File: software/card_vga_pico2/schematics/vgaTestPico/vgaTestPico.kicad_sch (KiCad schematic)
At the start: 31 parts, among them J10 Conn_02x37_Row_Letter_Last, U2 74HC138, U3 74HC139, U4 74HC245, U5 74HC245

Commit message: Schematic update
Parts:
- removed R5: 1k, symbol Device:R
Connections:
- net /AS is gone; now on net C./AS: R22.2
- net /LDS is gone; now on net C./LDS: R21.2
- net C.R/W: now also R20.2
- net /WRL: no longer R20.2
- net at U4.1 (A->B): now also U1.13 (GND), U1.18 (GND), U1.23 (GND), U1.28 (GND), U1.3 (GND), U1.33 (GND), U1.38 (GND), U1.8 (GND), U2.8 (GND), U3.13 (A1), U3.14 (A0), U3.15 (E), U3.8 (GND), U4.10 (GND), U4.19 (CE), U5.1 (A->B), U5.10 (GND), U5.11 (B7), U5.12 (B6), U5.13 (B5), U5.19 (CE), U5.7 (A5), U5.8 (A6), U5.9 (A7)
- net at U2.5 (~{E1}): now also U3.4 (O0)
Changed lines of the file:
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@@
 	)
 	(junction
+		(at 53.34 137.16)
+		(diameter 0)
+		(color 0 0 0 0)
+	)
+	(junction
 		(at 83.82 139.7)
 		(diameter 0)
@@
 	)
 	(junction
+		(at 53.34 142.24)
+		(diameter 0)
+		(color 0 0 0 0)
+	)
+	(junction
+		(at 83.82 147.32)
+		(diameter 0)
+		(color 0 0 0 0)
+	)
+	(junction
+		(at 83.82 99.06)
+		(diameter 0)
+		(color 0 0 0 0)
+	)
+	(junction
+		(at 53.34 139.7)
+		(diameter 0)
+		(color 0 0 0 0)
+	)
+	(junction
 		(at 83.82 137.16)
 		(diameter 0)
@@
 	(wire
 		(pts
-			(xy 83.82 142.24) (xy 83.82 149.86)
+			(xy 83.82 142.24) (xy 83.82 147.32)
 		)
 		(stroke
@@
 	(wire
 		(pts
+			(xy 83.82 96.52) (xy 83.82 99.06)
+		)
+		(stroke
+			(width 0)
+			(type default)
+		)
+	)
+	(wire
+		(pts
 			(xy 228.6 110.49) (xy 245.11 110.49)
 		)
@@
 	(wire
 		(pts
+			(xy 83.82 147.32) (xy 83.82 149.86)
+		)
+		(stroke
+			(width 0)
+			(type default)
+		)
+	)
+	(wire
+		(pts
 			(xy 33.02 124.46) (xy 39.37 124.46)
 		)
@@
 		)
 	)
+	(wire
+		(pts
+			(xy 81.28 96.52) (xy 83.82 96.52)
+		)
+		(stroke
+			(width 0)
+			(type default)
+		)
+	)
 	(bus
 		(pts
@@
 	(wire
 		(pts
+			(xy 53.34 142.24) (xy 53.34 160.02)
+		)
+		(stroke
+			(width 0)
+			(type default)
+		)
+	)
+	(wire
+		(pts
 			(xy 156.21 60.96) (xy 156.21 168.91)
 		)
@@
 		)
 	)
+	(wire
+		(pts
+			(xy 81.28 147.32) (xy 83.82 147.32)
+		)
+		(stroke
+			(width 0)
+			(type default)
+		)
+	)
 	(bus
 		(pts
@@
 		)
 	)
+	(wire
+		(pts
+			(xy 53.34 142.24) (xy 55.88 142.24)
+		)
+		(stroke
+			(width 0)
+			(type default)
+		)
+	)
 	(bus
 		(pts
@@
 	(wire
 		(pts
+			(xy 53.34 139.7) (xy 53.34 142.24)
+		)
+		(stroke
+			(width 0)
+			(type default)
+		)
+	)
+	(wire
+		(pts
 			(xy 228.6 46.99) (xy 245.11 46.99)
 		)
@@
 	(wire
 		(pts
-			(xy 186.69 78.74) (xy 190.5 78.74)
+			(xy 186.69 78.74) (xy 209.55 78.74)
 		)
 		(stroke
@@
 	(wire
 		(pts
+			(xy 53.34 137.16) (xy 55.88 137.16)
+		)
+		(stroke
+			(width 0)
+			(type default)
+		)
+	)
+	(wire
+		(pts
 			(xy 228.6 95.25) (xy 245.11 95.25)
 		)
@@
 	(wire
 		(pts
+			(xy 53.34 137.16) (xy 53.34 139.7)
+		)
+		(stroke
+			(width 0)
+			(type default)
+		)
+	)
+	(wire
+		(pts
 			(xy 81.28 81.28) (xy 104.14 81.28)
 		)
@@
 	(wire
 		(pts
-			(xy 228.6 64.77) (xy 245.11 64.77)
+			(xy 53.34 139.7) (xy 55.88 139.7)
 		)
 		(stroke
@@
 		)
 	)
-	(bus
+	(wire
 		(pts
-			(xy 226.06 92.71) (xy 226.06 95.25)
+			(xy 228.6 64.77) (xy 245.11 64.77)
 		)
 		(stroke
@@
 		)
 	)
-	(wire
+	(bus
 		(pts
-			(xy 198.12 78.74) (xy 209.55 78.74)
+			(xy 226.06 92.71) (xy 226.06 95.25)
 		)
 		(stroke
@@
 	(wire
 		(pts
-			(xy 53.34 106.68) (xy 53.34 160.02)
+			(xy 53.34 106.68) (xy 53.34 137.16)
 		)
 		(stroke
@@
 		)
 	)
-	(global_label "{slash}AS"
+	(global_label "C.{slash}AS"
 		(shape input)
 		(at 207.01 107.95 0)
@@
 		)
 		(property "Intersheetrefs" "${INTERSHEET_REFS}"
-			(at 213.6238 107.95 0)
-			(effects
-				(font
-					(size 1.27 1.27)
-				)
-				(justify left)
-				(hide yes)
-			)
-		)
-	)
-	(global_label "{slash}WRL"
-		(shape input)
-		(at 207.01 100.33 0)
-		(fields_autoplaced yes)
-		(effects
-			(font
-				(size 1.27 1.27)
-			)
-			(justify left)
-		)
-		(property "Intersheetrefs" "${INTERSHEET_REFS}"
-			(at 215.0752 100.33 0)
+			(at 215.4986 107.95 0)
 			(effects
 				(font
@@
 		)
 	)
-	(global_label "{slash}LDS"
+	(global_label "C.{slash}LDS"
 		(shape input)
 		(at 207.01 102.87 0)
@@
 		)
 		(property "Intersheetrefs" "${INTERSHEET_REFS}"
-			(at 214.8333 102.87 0)
+			(at 216.7081 102.87 0)
 			(effects
 				(font
@@
 		)
 	)
+	(global_label "C.R{slash}W"
+		(shape input)
+		(at 207.01 100.33 0)
+		(fields_autoplaced yes)
+		(effects
+			(font
+				(size 1.27 1.27)
+			)
+			(justify left)
+		)
+		(property "Intersheetrefs" "${INTERSHEET_REFS}"
+			(at 215.9219 100.33 0)
+			(effects
+				(font
+					(size 1.27 1.27)
+				)
+				(justify left)
+				(hide yes)
+			)
+		)
+	)
 	(hierarchical_label "A[1..23]"
 		(shape input)
@@
 					(unit 1)
 				)
-			)
-		)
-	)
-	(symbol
-		(lib_id "Device:R")
-		(at 194.31 78.74 90)
-		(unit 1)
-		(exclude_from_sim no)
-		(in_bom yes)
-		(on_board yes)
-		(dnp no)
-		(property "Reference" "R5"
-			(at 190.5 77.47 90)
-			(effects
-				(font
-					(size 1.27 1.27)
-				)
-			)
-		)
-		(property "Value" "1k"
-			(at 194.31 78.74 90)
-			(effects
-				(font
-					(size 1.27 1.27)
-				)
-			)
-		)
-		(property "Footprint" ""
-			(at 194.31 80.518 90)
-			(effects
-				(font
-					(size 1.27 1.27)
-				)
-				(hide yes)
-			)
-		)
-		(property "Datasheet" "~"
-			(at 194.31 78.74 0)
-			(effects
-				(font
-					(size 1.27 1.27)
-				)
-				(hide yes)
-			)
-		)
-		(property "Description" "Resistor"
-			(at 194.31 78.74 0)
-			(effects
-				(font
-					(size 1.27 1.27)
-				)
-				(hide yes)
-			)
-		)
-		(pin "2"
-		)
-		(pin "1"
-		)
-		(instances
-			(project "vgaTestPico"
-				(path "/7afca5d4-78c3-4891-b909-50f3d4b29fac"
-					(reference "R5")
-					(unit 1)
-				)

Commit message: updating
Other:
- note added: "pino 1 (A0) = A15 do 68000 pino 2 (A1) = A16 do 68000 pino 3 (A2) = A17 do 68000 pino 4 (/E0) = A18 do 68000 pino 5 (/E1) = /LDS R/W /AS do 68000 pino 6 (E2) = A19 do 68000 com isso a saida pino 7 /Y7 só deve ser acessada com 0xB8000"
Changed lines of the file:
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@@
+		)
+	)
+	(text "pino 1 (A0)  = A15 do 68000\npino 2 (A1)  = A16 do 68000\npino 3 (A2)  = A17 do 68000\npino 4 (/E0) = A18 do 68000\npino 5 (/E1) = /LDS R/W /AS do 68000\npino 6 (E2)  = A19 do 68000\n\ncom isso a saida pino 7 /Y7 só deve ser acessada com 0xB8000"
+		(exclude_from_sim no)
+		(at 183.896 37.846 0)
+		(effects
+			(font
+				(size 1.27 1.27)
+			)
 		)
 	)

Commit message: vga mode changing well
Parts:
- added U6: 24LC256, symbol Memory_EEPROM:24LC256
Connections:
- net at U1.13 (GND), U1.18 (GND), U1.23 (GND)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: now also U6.1 (A0), U6.2 (A1), U6.3 (A2), U6.4 (GND), U6.7 (WP)
- net at U1.36 (3V3(OUT)), U2.16 (VCC), U3.16 (VCC)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: now also U6.8 (VCC)
- net SDA: now reaches U1.19 (GP14)
- net SDA: now also U6.5 (SDA)
- net SCL: now reaches U1.20 (GP15)
- net SCL: now also U6.6 (SCL)

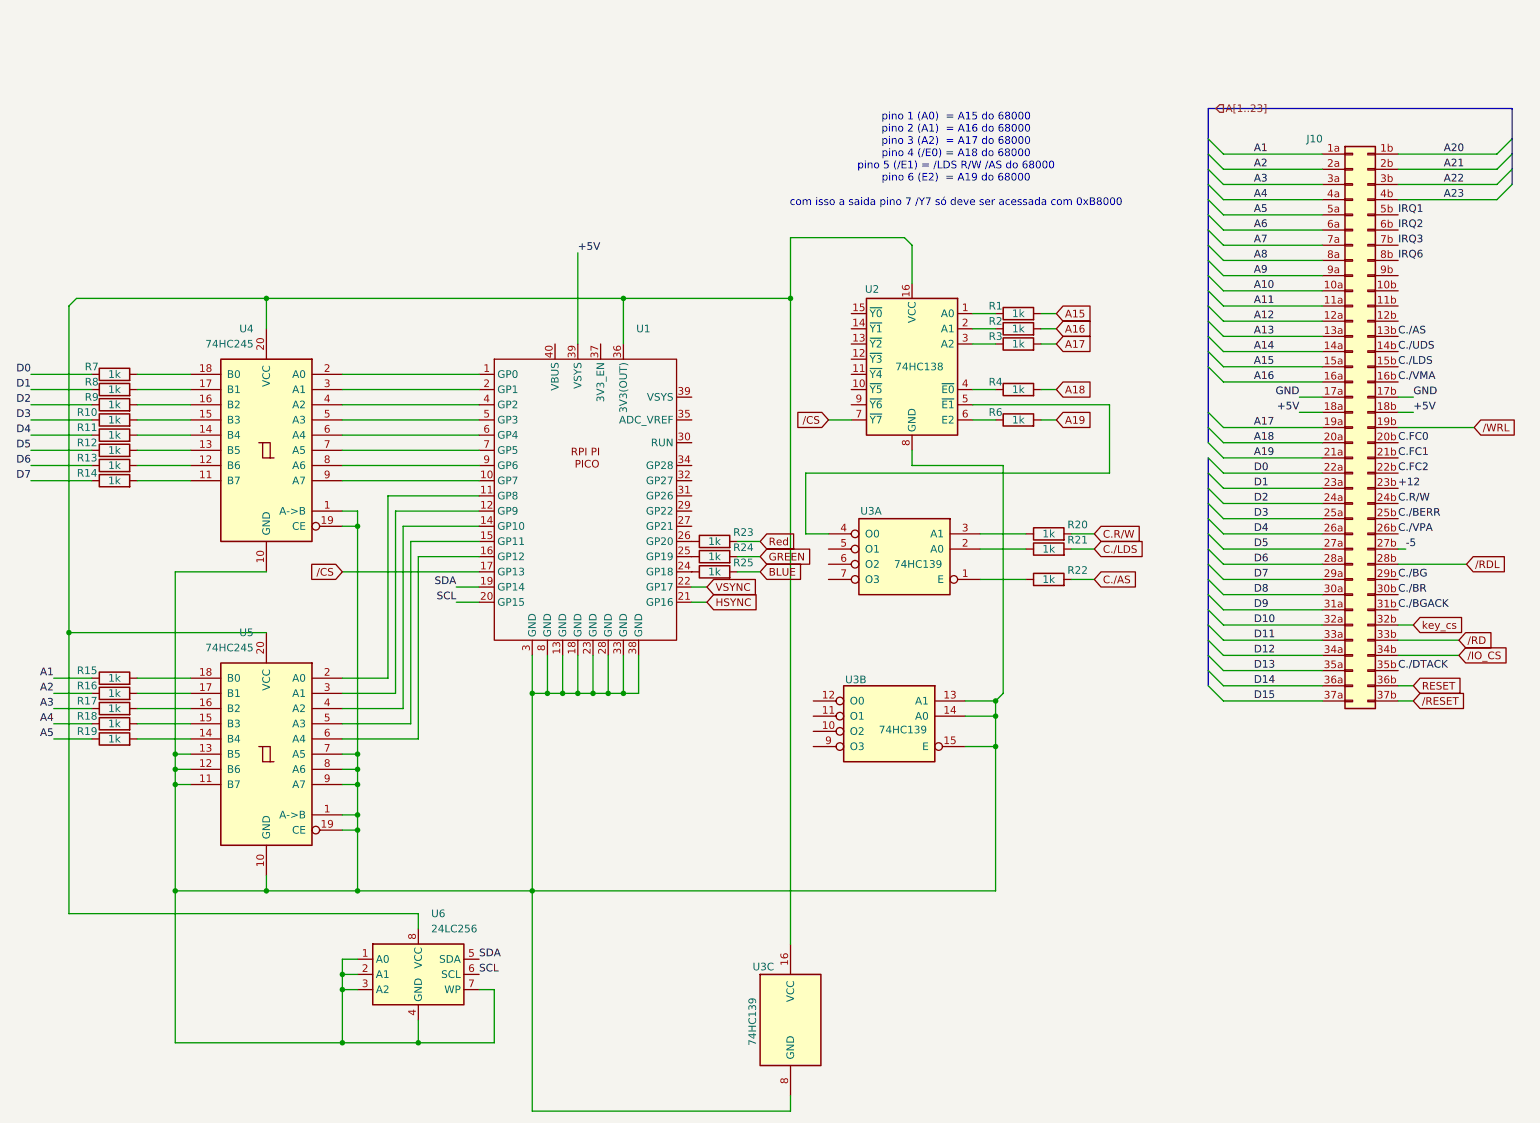
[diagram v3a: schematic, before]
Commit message: Added ch376s
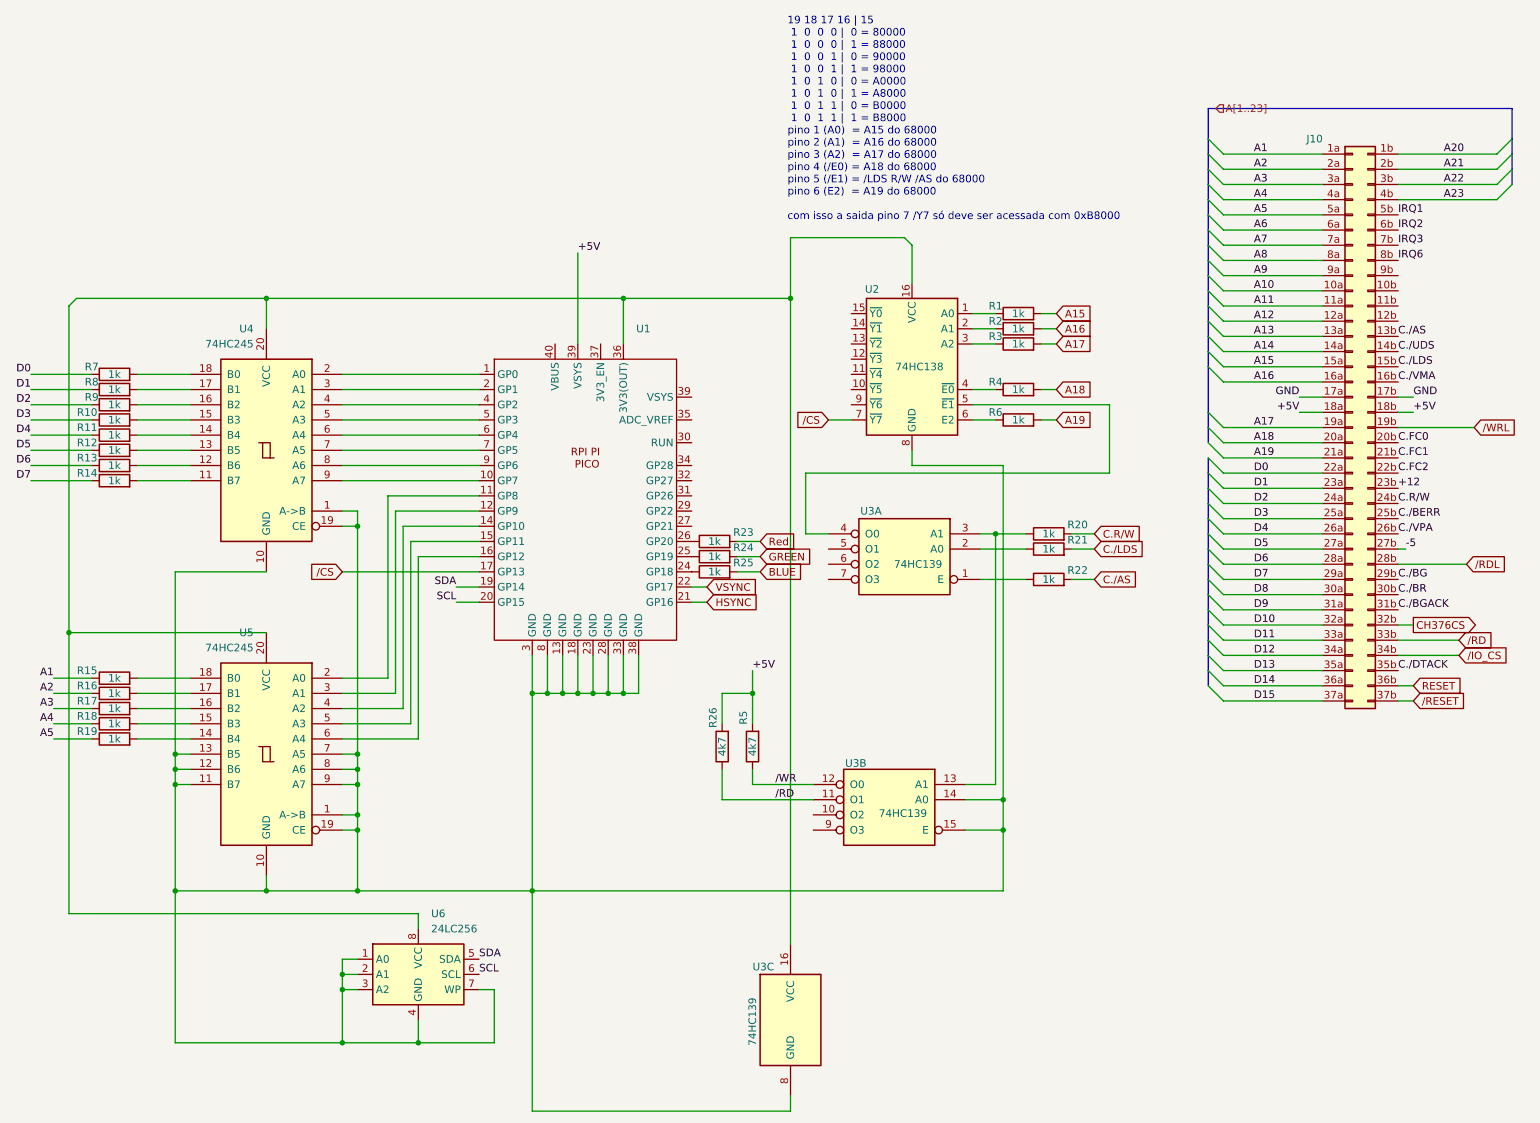
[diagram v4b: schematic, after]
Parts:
- added R26, R5: 4k7, symbol Device:R
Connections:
- net +5V: now also R26.2, R5.2
- net /RD: now also U3.11 (O1), R26.1
- net at U1.13 (GND), U1.18 (GND), U1.23 (GND)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: no longer U3.13 (A1)
- net at R20.1, U3.3 (A1): now also U3.13 (A1)
- net /WR: now reaches U3.12 (O0)
- net /WR: now also R5.1
- net key_cs renamed CH376CS
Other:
- note added: "19 18 17 16 | 15 1 0 0 0 | 0 = 80000 1 0 0 0 | 1 = 88000 1 0 0 1 | 0 = 90000 1 0 0 1 | 1 = 98000 1 0 1 0 | 0 = A0000 1 0 1 0 | 1 = A8000 1 0 1 1 | 0 = B0000 1 0 1 1 | 1 = B8000 pino 1 (A0) = A15 do 68000 pino 2 (A1) = A16 do 68000 pino 3 (A2) = A17 do 68000 pino 4 (/E0) = A18 do 68000 pino 5 (/E1) = /LDS R/W /AS do 68000 pino 6 (E2) = A19 do 68000 com isso a saida pino 7 /Y7 só deve ser acessada 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"
- note removed: "pino 1 (A0) = A15 do 68000 pino 2 (A1) = A16 do 68000 pino 3 (A2) = A17 do 68000 pino 4 (/E0) = A18 do 68000 pino 5 (/E1) = /LDS R/W /AS do 68000 pino 6 (E2) = A19 do 68000 com isso a saida pino 7 /Y7 só deve ser acessada com 0xB8000"
- moved on the sheet: U3B
